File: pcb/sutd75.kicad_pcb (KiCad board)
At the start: 2 copper layers, 340 x 135 mm, 219 parts, among them J1 SWD Header, J2 UART header, J3 USB_C_Receptacle_USB2.0, J4 I2C header, SW1 BOOT0, SW10 Tab, SW11 CapsLock, SW12 Shift, SW13 Ctrl, SW14 F1, SW15 1, SW16 Q, SW17 A, SW18 Z, SW19 Win, SW2 BOOT1, SW20 F2, SW21 2, SW22 W, SW23 S, SW24 X, SW25 F3, SW26 3, SW27 E, SW28 D, SW29 C, SW3 RESET, SW30 F4, SW31 4, SW32 R, SW33 F, SW34 V, SW35 F5, SW36 5, SW37 T, SW38 G, SW39 B, SW4 M1, SW40 Space, SW41 F6, SW42 6, SW43 Y, SW44 H, SW45 N, SW46 F7, SW47 7, SW48 U, SW49 J, SW5 M2, SW50 M, SW51 F8, SW52 8, SW53 I, SW54 K, SW55 Comma, SW56 RAlt, SW57 F9, SW58 9, SW59 O, SW6 M3, SW60 L, SW61 Period, SW62 RFn, SW63 F10, SW64 0, SW65 P, SW66 Semicolon, SW67 Slash, SW68 RCtrl, SW69 F11, SW7 M4, SW70 Minus, SW71 LBrkt, SW72 Quote, SW73 RShift, SW74 F12, SW75 Equals, SW76 RBrkt, SW77 Enter, SW78 LArr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

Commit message: Add keyboard layout to pcb layout
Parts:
- added D96: D, Diode_SMD:D_SOD-323, B.Cu at (106.8, 220.4)
- added SW91: Alt, Switch_Keyboard_Kailh:SW_Hotswap_Kailh_MX_plated_1.25u, F.Cu at (130.6, 216.2)
- SW10, SW11, SW12, SW14, SW15, SW16, SW17, SW18, SW20, SW21, SW22, SW23, SW24, SW25, SW26, SW27, SW28, SW29, SW30, SW31, SW32, SW33, SW34, SW35, SW36, SW37, SW38, SW39, SW41, SW42, SW43, SW44, SW45, SW46, SW47, SW48, SW49, SW50, SW51, SW52, SW53, SW54, SW55, SW57, SW58, SW59, SW60, SW61, SW63, SW64, SW65, SW66, SW67, SW69, SW70, SW71, SW74, SW76, SW77, SW78, SW79, SW8, SW82, SW83, SW84, SW85, SW86, SW87, SW88, SW89, SW9: footprint Switch_Keyboard_Kailh:SW_Hotswap_Kailh_1.00u -> Switch_Keyboard_Kailh:SW_Hotswap_Kailh_MX_plated_1.00u
- SW13, SW19, SW7: footprint Switch_Keyboard_Kailh:SW_Hotswap_Kailh_1.25u -> Switch_Keyboard_Kailh:SW_Hotswap_Kailh_MX_plated_1.25u
- SW4: footprint Switch_Keyboard_Kailh:SW_Hotswap_Kailh_1.50u -> Switch_Keyboard_Kailh:SW_Hotswap_Kailh_MX_plated_1.50u
- SW40: footprint Switch_Keyboard_Kailh:SW_Hotswap_Kailh_2.25u -> Switch_Keyboard_Kailh:SW_Hotswap_Kailh_MX_plated_6.25u
- SW5: footprint Switch_Keyboard_Kailh:SW_Hotswap_Kailh_1.75u_SteppedCapsLock -> Switch_Keyboard_Kailh:SW_Hotswap_Kailh_MX_1.75u_SteppedCapsLock
- SW56, SW62, SW68, SW72: footprint Switch_Keyboard_Kailh:SW_Hotswap_Kailh_1.25u -> Switch_Keyboard_Kailh:SW_Hotswap_Kailh_MX_plated_1.00u
- SW6: footprint Switch_Keyboard_Kailh:SW_Hotswap_Kailh_2.25u -> Switch_Keyboard_Kailh:SW_Hotswap_Kailh_MX_plated_2.25u
- SW73: footprint Switch_Keyboard_Kailh:SW_Hotswap_Kailh_1.75u -> Switch_Keyboard_Kailh:SW_Hotswap_Kailh_MX_plated_1.75u
- SW75: footprint Switch_Keyboard_Kailh:SW_Hotswap_Kailh_2.00u -> Switch_Keyboard_Kailh:SW_Hotswap_Kailh_MX_1.00u
- SW80: footprint Switch_Keyboard_Kailh:SW_Hotswap_Kailh_1.00u -> Switch_Keyboard_Kailh:SW_Hotswap_Kailh_MX_plated_2.00u
- SW81: footprint Switch_Keyboard_Kailh:SW_Hotswap_Kailh_1.00u -> Switch_Keyboard_Kailh:SW_Hotswap_Kailh_MX_plated_1.50u
- moved SW68 266.8 mm to (309.2, 216.2)
- moved SW62 253.3 mm to (290.2, 216.2)
- moved SW75 224.1 mm to (309.2, 140.0)
- moved SW40 211.3 mm to (202.1, 216.2)
- moved SW74 209.7 mm to (323.5, 116.2)
- moved SW69 209.5 mm to (304.5, 116.2)
- moved SW10 203.5 mm to (85.4, 159.1)
- moved SW72 198.3 mm to (304.5, 178.2)
- moved SW77 191.7 mm to (323.5, 84.8)
- moved SW14 190.3 mm to (104.5, 116.2)
- moved SW56 189.0 mm to (271.1, 216.2)
- moved SW54 177.5 mm to (247.3, 178.2)
- moved SW9 172.5 mm to (80.6, 140.0)
- moved SW81 171.4 mm to (342.6, 159.1)
- moved SW15 170.6 mm to (99.7, 140.0)
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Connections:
- SW75 pad 1: /COL14 -> Net-(D81-Pad1)
- SW75 pad 2: Net-(D81-Pad1) -> /COL14

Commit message: Arrange the rest of the switches
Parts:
- added C15: 100nF, Capacitor_SMD:C_0402_1005Metric, B.Cu at (128.4, 65.8)
- C1, C10, C11, C12, C13, C14, C2, C3, C4, C5, C6, C7, C8, C9, D1, D10, D11, D12, D13, D14, D15, D16, D17, D18, D19, D2, D20, D21, D22, D23, D24, D25, D26, D27, D28, D29, D3, D30, D31, D32, D33, D34, D35, D36, D37, D38, D39, D4, D40, D41, D42, D43, D44, D45, D46, D47, D48, D49, D5, D50, D51, D52, D53, D54, D55, D56, D57, D58, D59, D6, D60, D61, D62, D63, D64, D65, D66, D67, D68, D69, D7, D70, D71, D72, D73, D74, D75, D76, D77, D78, D79, D8, D80, D82, D83, D84, D85, D86, D87, D88, D89, D9, D90, D91, D92, D93, D94, D95, H4, J1, J2, J3, J4, JP1, R1, R2, R3, R4, R5, R6, SW1, SW2, SW3, U1, U2, U3, XTAL1, XTAL2: moved to B.Cu
- SW10: footprint Switch_Keyboard_Kailh:SW_Hotswap_Kailh_MX_plated_1.00u -> Switch_Keyboard_Kailh:SW_Hotswap_Kailh_MX_plated_1.50u
- SW11: footprint Switch_Keyboard_Kailh:SW_Hotswap_Kailh_MX_plated_1.00u -> Switch_Keyboard_Kailh:SW_Hotswap_Kailh_MX_1.75u_SteppedCapsLock
- SW12, SW77: footprint Switch_Keyboard_Kailh:SW_Hotswap_Kailh_MX_plated_1.00u -> Switch_Keyboard_Kailh:SW_Hotswap_Kailh_MX_plated_2.25u
- SW4: footprint Switch_Keyboard_Kailh:SW_Hotswap_Kailh_MX_plated_1.50u -> Switch_Keyboard_Kailh:SW_Hotswap_Kailh_MX_plated_1.00u
- SW5: footprint Switch_Keyboard_Kailh:SW_Hotswap_Kailh_MX_1.75u_SteppedCapsLock -> Switch_Keyboard_Kailh:SW_Hotswap_Kailh_MX_plated_1.00u
- SW6: footprint Switch_Keyboard_Kailh:SW_Hotswap_Kailh_MX_plated_2.25u -> Switch_Keyboard_Kailh:SW_Hotswap_Kailh_MX_plated_1.00u
- SW7: footprint Switch_Keyboard_Kailh:SW_Hotswap_Kailh_MX_plated_1.25u -> Switch_Keyboard_Kailh:SW_Hotswap_Kailh_MX_plated_1.00u
- SW75: footprint Switch_Keyboard_Kailh:SW_Hotswap_Kailh_MX_1.00u -> Switch_Keyboard_Kailh:SW_Hotswap_Kailh_MX_plated_1.00u
- moved D94 374.6 mm to (375.9, 202.9), turned to 180 degrees
- moved D88 361.9 mm to (352.1, 207.7), turned to 180 degrees
- moved D84 351.2 mm to (333.1, 226.7), turned to 180 degrees
- moved H3 350.9 mm to (335.4, 178.2)
- moved SW90 348.1 mm to (375.9, 116.2), turned to -90 degrees
- moved SW89 347.2 mm to (371.1, 221.0)
- moved D83 334.4 mm to (335.4, 183.9), turned to 180 degrees
- moved D68 326.4 mm to (290.2, 222.0), turned to 180 degrees
- moved SW73 325.3 mm to (321.1, 197.2)
- moved SW88 325.0 mm to (375.9, 197.2)
- moved H2 322.6 mm to (202.1, 216.2)
- moved H4 318.8 mm to (337.8, 140.0), turned to 180 degrees
- moved D81 307.5 mm to (309.2, 145.8), turned to 180 degrees
- moved D86 306.1 mm to (337.8, 145.8), turned to 180 degrees
- moved SW82 303.6 mm to (352.1, 202.0)
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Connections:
- D2 pad 4: /RGBLED_DOUT -> unconnected-(D2-Pad4)
- D81 pad 1: Net-(D81-Pad1) -> Net-(SW75-Pad2)
- SW75 pad 1: Net-(D81-Pad1) -> /COL14
- SW75 pad 2: /COL14 -> Net-(SW75-Pad2)
- U2 pad 41: /INDICATOR_LED -> unconnected-(U2-Pad41)
- U2 pad 64: unconnected-(U2-Pad64) -> +3V3
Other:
- board size 340 x 135 mm -> 348.1 x 133.8 mm

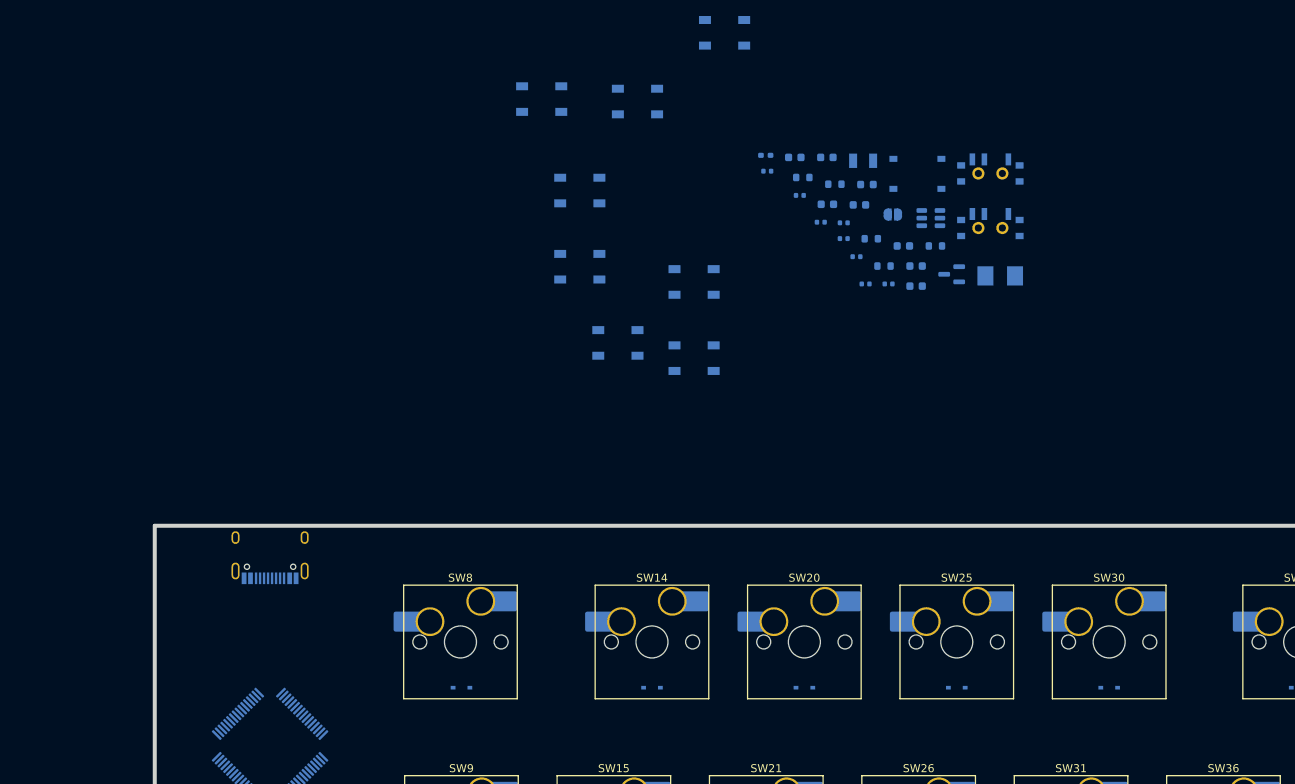
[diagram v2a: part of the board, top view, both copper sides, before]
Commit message: Group some of the components together first
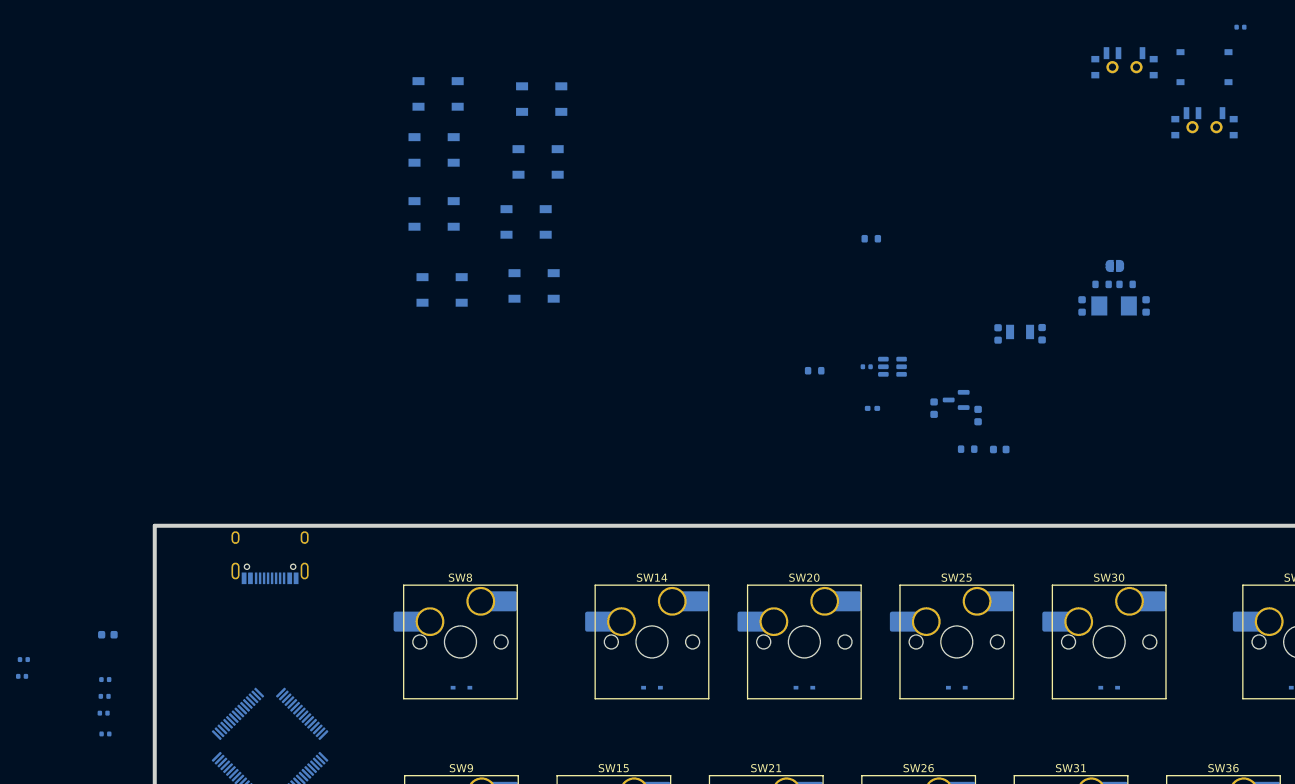
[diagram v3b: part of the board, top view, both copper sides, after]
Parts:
- moved C12 116.3 mm to (25.7, 120.5)
- moved C13 113.0 mm to (25.9, 118.4)
- moved C15 111.1 mm to (36.1, 127.7)
- moved C5 111.0 mm to (36.4, 115.3)
- moved C11 110.0 mm to (35.9, 125.1)
- moved C6 109.7 mm to (36.1, 120.9)
- moved C10 105.7 mm to (36.0, 123.0)
- moved C7 57.8 mm to (178.0, 39.4)
- moved R2 42.6 mm to (163.7, 71.5)
- moved D8 39.2 mm to (77.2, 54.7)
- moved SW3 38.3 mm to (173.5, 44.4)
- moved C9 38.0 mm to (153.2, 77.7), turned to 90 degrees
- moved D1 37.0 mm to (147.9, 92.2)
- moved R3 37.0 mm to (143.9, 92.1)
- moved R6 34.3 mm to (132.0, 87.0)
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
